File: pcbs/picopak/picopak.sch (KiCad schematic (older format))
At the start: 34 parts, among them J1 USB_B_Micro, J2 Conn_02x08_Odd_Even, J3 Conn_01x03_Female, J4 Conn_01x04_Female, SW1 sw, SW2 sw, SW3 sw, SW4 sw, U1 NCP1117-3.3_SOT223, U10 74LS245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

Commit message: Second PCB with errata fixed added
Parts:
- C4: footprint Capacitor_SMD:C_0805_2012Metric -> Capacitor_SMD:C_0402_1005Metric
- U3: symbol MCU_RaspberryPi_RP2040:RP2040 -> picopak-rescue:RP2040-MCU_RaspberryPi_RP2040
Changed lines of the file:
@@
 $EndDescr
 $Comp
-L MCU_RaspberryPi_RP2040:RP2040 U3
+L picopak-rescue:RP2040-MCU_RaspberryPi_RP2040 U3
 U 1 1 5ED8F5D6
 P 7800 5700
@@
 F 0 "C4" H 3815 1996 50  0000 L CNN
 F 1 "10u" H 3815 1905 50  0000 L CNN
-F 2 "Capacitor_SMD:C_0805_2012Metric" H 3738 1800 50  0001 C CNN
+F 2 "Capacitor_SMD:C_0402_1005Metric" H 3738 1800 50  0001 C CNN
 F 3 "~" H 3700 1950 50  0001 C CNN
 	1    3700 1950
@@
 L Connector:Conn_01x04_Female J?
 U 1 1 613957E3
-P 9325 9825
+P 9325 9725
 AR Path="/6104FF77/613957E3" Ref="J?"  Part="1"
 AR Path="/613957E3" Ref="J4"  Part="1"
-F 0 "J4" H 9217 10110 50  0000 C CNN
-F 1 "Conn_01x04_Female" H 9217 10019 50  0000 C CNN
-F 2 "ajm_kicad:OLED_SMALL" H 9325 9825 50  0001 C CNN
-F 3 "~" H 9325 9825 50  0001 C CNN
-	1    9325 9825
-	-1   0    0    1
+F 0 "J4" H 9217 10010 50  0000 C CNN
+F 1 "Conn_01x04_Female" H 9217 9919 50  0000 C CNN
+F 2 "ajm_kicad:OLED_SMALL" H 9325 9725 50  0001 C CNN
+F 3 "~" H 9325 9725 50  0001 C CNN
+	1    9325 9725
+	-1   0    0    -1
 $EndComp
 $Comp
@@
 	9525 9925 9900 9925
 Wire Wire Line
-	9525 9725 11250 9725
+	9525 9725 10900 9725
 Wire Wire Line
 	9525 9625 10400 9625
@@
 Connection ~ 10400 9625
 Wire Wire Line
-	10900 9500 10900 9625
-Wire Wire Line
-	10400 9625 10900 9625
-Connection ~ 10900 9625
-Wire Wire Line
-	10900 9625 11250 9625
-Wire Wire Line
 	9950 9075 9950 9200
 Wire Wire Line
@@
 Wire Wire Line
 	9950 9200 9950 9825
+Wire Wire Line
+	10400 9625 11250 9625
+Wire Wire Line
+	10900 9500 10900 9725
+Connection ~ 10900 9725
+Wire Wire Line
+	10900 9725 11250 9725
 $EndSCHEMATC

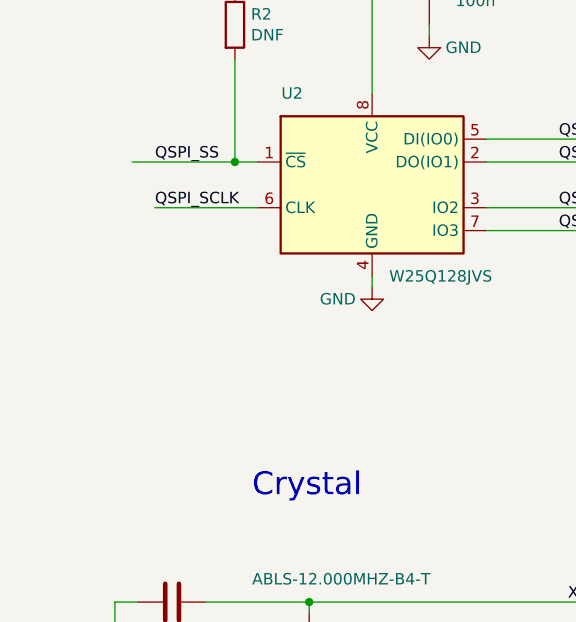
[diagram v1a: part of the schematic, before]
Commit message: Added RUN jumper for drag-drop upgrade, SWD pads moved
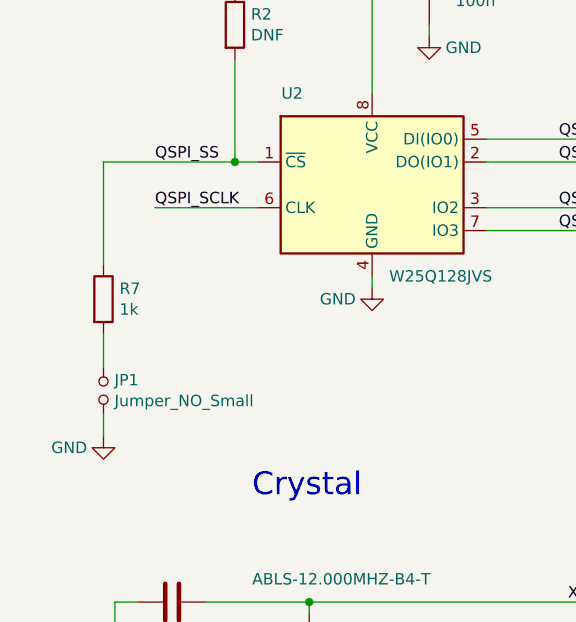
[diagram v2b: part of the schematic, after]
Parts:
- added JP1: Jumper_NO_Small, Jumper:SolderJumper-2_P1.3mm_Open_Pad1.0x1.5mm, symbol Device:Jumper_NO_Small
- added R7: 1k, Capacitor_SMD:C_0402_1005Metric, symbol Device:R
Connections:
- wire segments 184 -> 187
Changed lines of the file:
@@
 Wire Wire Line
 	1150 8275 1600 8275
-Wire Wire Line
-	1050 8075 1500 8075
 Text Label 1150 8275 0    50   ~ 0
 QSPI_SCLK
@@
 Wire Wire Line
 	10900 9725 11250 9725
+$Comp
+L Device:R R7
+U 1 1 6131CA53
+P 925 8675
+F 0 "R7" H 995 8721 50  0000 L CNN
+F 1 "1k" H 995 8630 50  0000 L CNN
+F 2 "Capacitor_SMD:C_0402_1005Metric" V 855 8675 50  0001 C CNN
+F 3 "~" H 925 8675 50  0001 C CNN
+	1    925  8675
+	1    0    0    -1
+$EndComp
+Wire Wire Line
+	925  8075 925  8525
+Wire Wire Line
+	925  8075 1500 8075
+$Comp
+L Device:Jumper_NO_Small JP1
+U 1 1 6132F30C
+P 925 9075
+F 0 "JP1" V 879 9123 50  0000 L CNN
+F 1 "Jumper_NO_Small" V 970 9123 50  0000 L CNN
+F 2 "Jumper:SolderJumper-2_P1.3mm_Open_Pad1.0x1.5mm" H 925 9075 50  0001 C CNN
+F 3 "~" H 925 9075 50  0001 C CNN
+	1    925  9075
+	0    1    1    0
+$EndComp
+$Comp
+L power:GND #PWR02
+U 1 1 6133032E
+P 925 9275
+F 0 "#PWR02" H 925 9025 50  0001 C CNN
+F 1 "GND" H 775 9225 50  0000 C CNN
+F 2 "" H 925 9275 50  0001 C CNN
+F 3 "" H 925 9275 50  0001 C CNN
+	1    925  9275
+	1    0    0    -1
+$EndComp
+Wire Wire Line
+	925  8825 925  8975
+Wire Wire Line
+	925  9175 925  9275
 $EndSCHEMATC

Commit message: V1_2 PCB laid out
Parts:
- added D1: PMEG3010ER, Diode_SMD:D_SOD-123, symbol Device:D
- added J5: Conn_01x02_Female, Connector_PinHeader_1.00mm:PinHeader_1x02_P1.00mm_Vertical_SMD_Pin1Left, symbol Connector:Conn_01x02_Female
- added R8, R9: R_Small, Capacitor_SMD:C_0402_1005Metric, symbol Device:R_Small
- added TR1: Si2302CDS-n-channel, Package_TO_SOT_SMD:SOT-23, symbol New_Library:Si2302CDS-n-channel
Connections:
- net GND: now also R9.2
- net BATSENSE: now reaches U3.41 (GPIO29_ADC3)
- net BATSENSE: now also R8.2, R9.1
- net VBUS: no longer names the net of C1.1, U1.3 (VI)
- net VBUS: now also D1.1 (K), TR1.2 (S); no longer J1.1 (VBUS)
- new net: D1.2 (A), J1.1 (VBUS)
- new net: J5.1 (Pin_1), TR1.1 (G)
- new net: J5.2 (Pin_2), R8.1, TR1.3 (D)
- no-connect marks 1 -> 14
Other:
- note added: "VBat from \norganiser"
- note added: "VLCD"
- moved on the sheet: C1, C4, J1, U1

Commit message: Updates. Archive file for PCB
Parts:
- added M1: Si2301 P chan, Package_TO_SOT_SMD:SOT-23, symbol GeekAmmo:P-CHANNEL-MOSFET
- added R10: 10k, Capacitor_SMD:C_0402_1005Metric, symbol Device:R_Small
- added R11: 100k, Capacitor_SMD:C_0402_1005Metric, symbol Device:R_Small
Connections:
- net GND: now also TR1.2 (S)
- net at C1.1, D1.1 (K), U1.3 (VI): now also M1.3 (D); no longer TR1.2 (S)
- net at TR1.1 (G): now also R10.1; no longer J5.1 (Pin_1)
- net at J5.2 (Pin_2), R8.1: now also M1.2 (S), R11.1; no longer TR1.3 (D)
- new net: M1.1 (G), R11.2, TR1.3 (D)
- new net: J5.1 (Pin_1), R10.2
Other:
- moved on the sheet: C1, C4, D1, J1, J3, J5, R8, R9, TR1, U1, XS1
